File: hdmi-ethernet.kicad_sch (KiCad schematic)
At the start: 123 parts

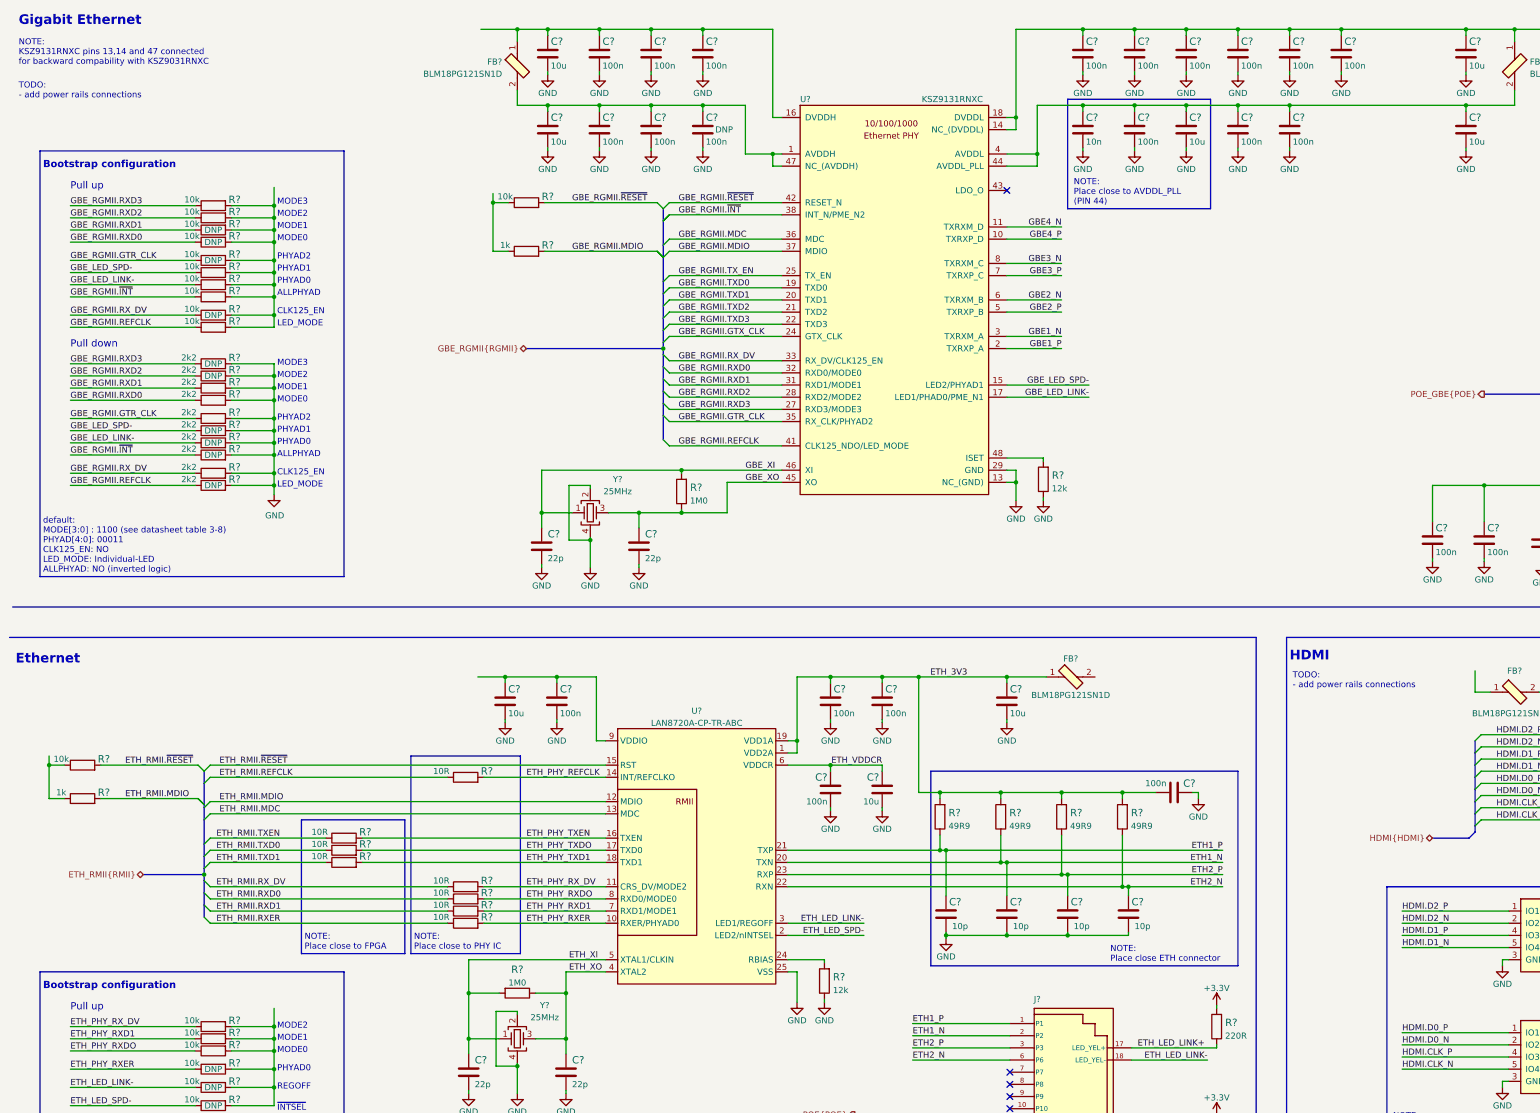
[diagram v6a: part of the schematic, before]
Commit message: Add missing labels on ISET and internal power rails. Update GBE bootstrap config info
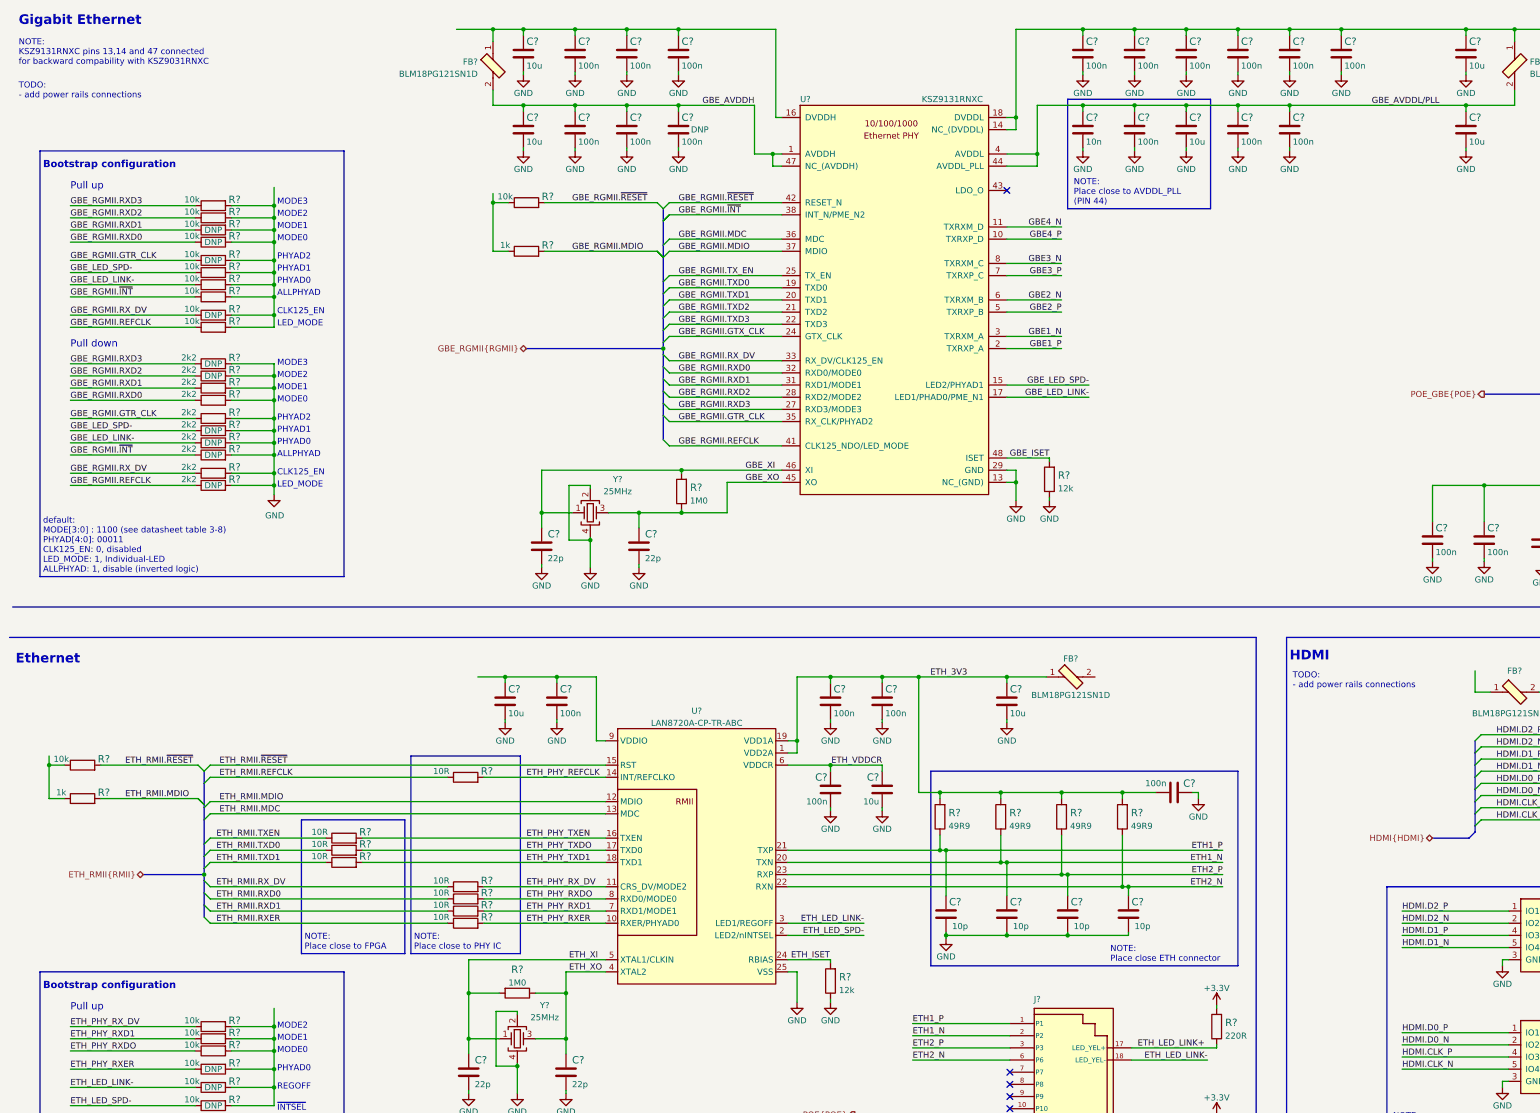
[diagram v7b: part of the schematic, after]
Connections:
- net ETH_ISET: now reaches R?.2, U?.24 (RBIAS)
- net GBE_ISET: now reaches R?.2, U?.48 (ISET)
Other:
- note added: "default: MODE[3:0] : 1100 (see datasheet table 3-8) PHYAD[4:0]: 00011 CLK125_EN: 0, disabled LED_MODE: 1, Individual-LED ALLPHYAD: 1, disable (inverted logic)"
- note removed: "default: MODE[3:0] : 1100 (see datasheet table 3-8) PHYAD[4:0]: 00011 CLK125_EN: NO LED_MODE: Individual-LED ALLPHYAD: NO (inverted logic)"
- moved on the sheet: C?, FB?, R?

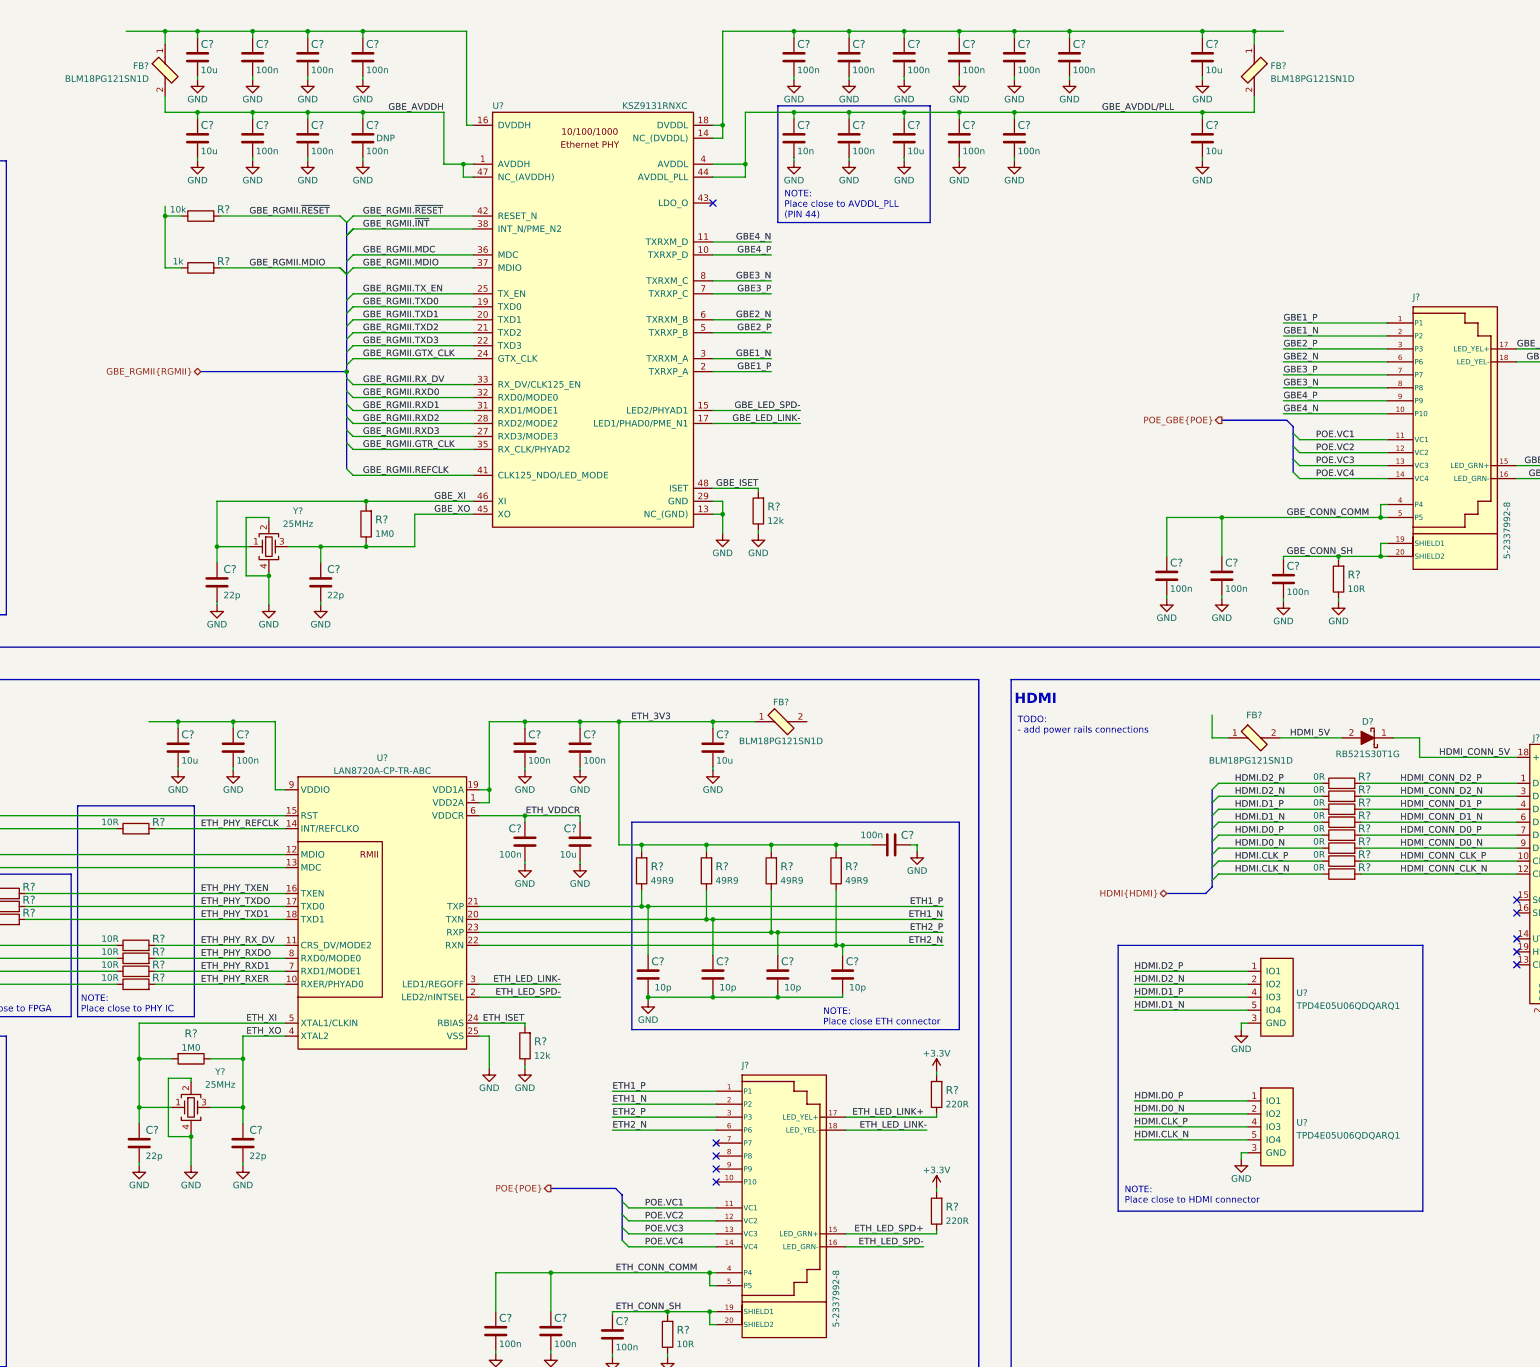
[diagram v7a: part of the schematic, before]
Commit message: Add missing DCT 0R, connect 3.3V rail to LAN8720A
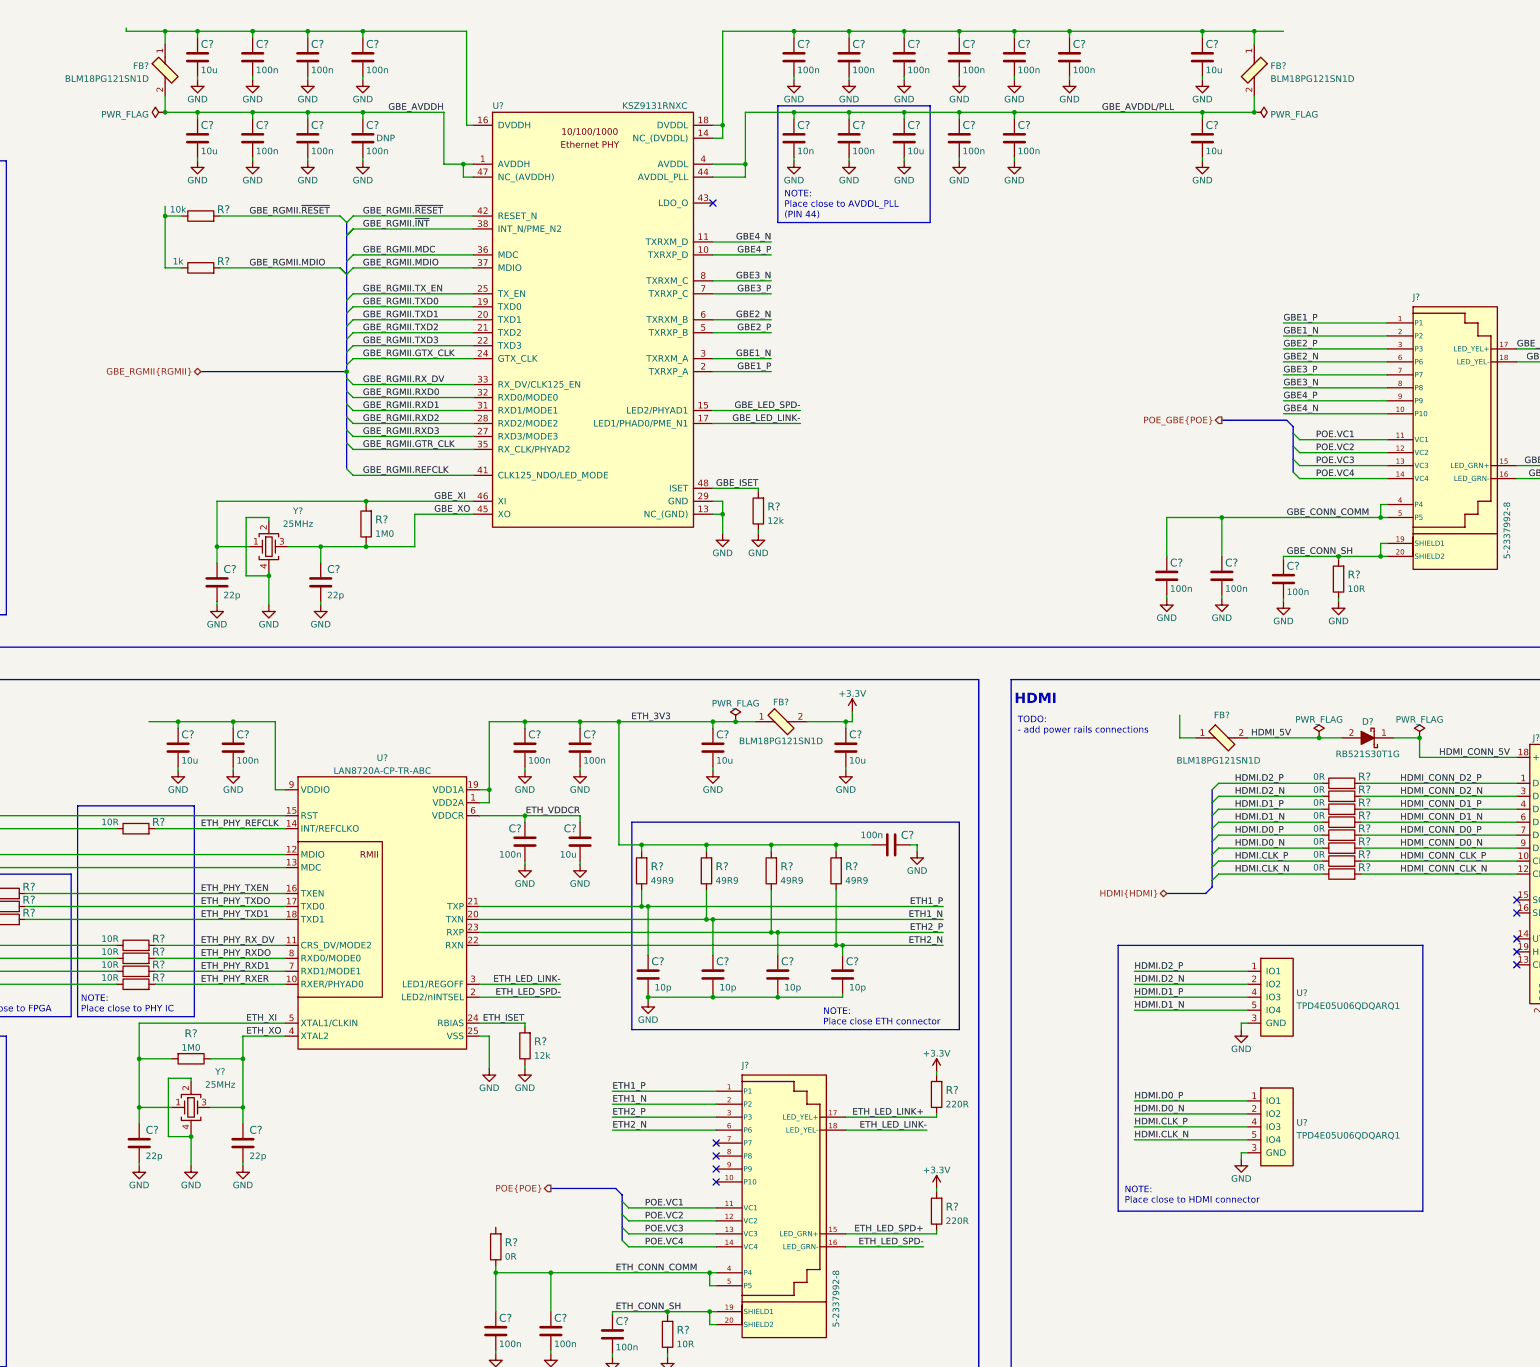
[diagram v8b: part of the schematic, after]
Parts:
- added C?: C_10u_0402, antmicro-footprints:0402-cap, symbol antmicroCapacitors0402:C_10u_0402
- added R?: R_0R_0402, antmicro-footprints:0402-res, symbol antmicroResistors0402:R_0R_0402
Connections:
- net +3V3: now also FB?.2, C?.1
- net ETH_CONN_COMM: now also R?.1
- net GND: now also C?.2
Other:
- moved on the sheet: FB?
